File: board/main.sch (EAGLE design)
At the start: 58 parts, among them IC1 ATMEGA48/88/168-AU, IC2 LM386N-1, J1 AVR_SPI_PRG_6PTH, Q2 MOSFET-NCHANNELSMD, Q3 MOSFET-NCHANNELSMD, U1 AT24C1024B-8S2, U2 AT24C1024B-8S2

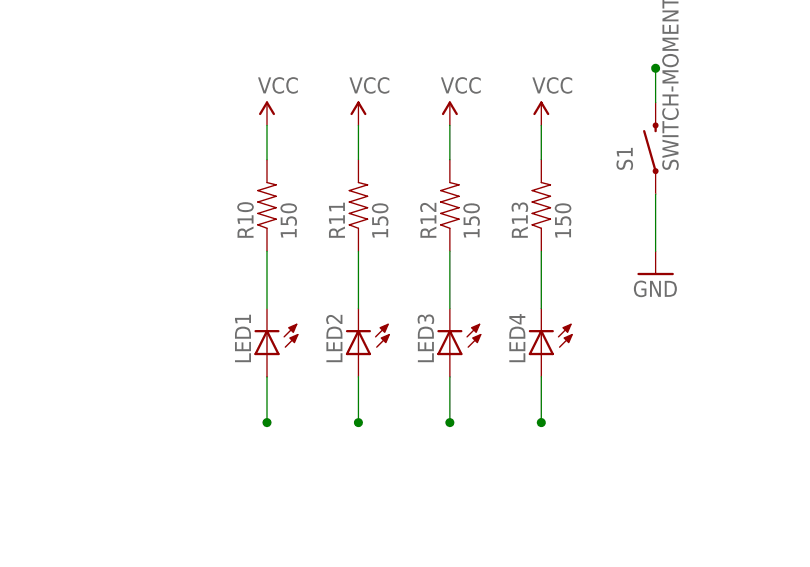
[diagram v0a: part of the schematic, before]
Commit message: Fixed the TWI interface
Seems there was a problem with the waiting for-i2c-logic.  Fixed and now it's working.  Yippie.  SO MUCH WASTED TIME.  Ugh.
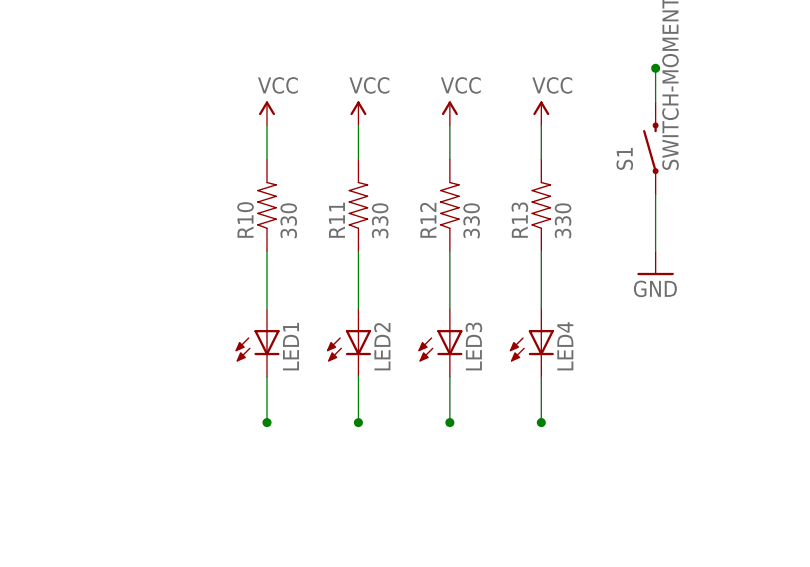
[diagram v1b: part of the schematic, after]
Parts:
- R10, R11, R12, R13: value 150 -> 330
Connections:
- net LED1: now also LED1.C; no longer LED1.A
- net LED2: now also LED2.C; no longer LED2.A
- net LED3: now also LED3.C; no longer LED3.A
- net LED4: now also LED4.C; no longer LED4.A
- net N$10: now also LED1.A, R10.1; no longer LED4.C, R13.1
- net N$11: now also LED2.A, R11.1; no longer LED3.C, R12.1
- net N$13: now also LED3.A, R12.1; no longer LED2.C, R11.1
- net N$14: now also LED4.A, R13.1; no longer LED1.C, R10.1
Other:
- moved on the sheet: LED1, LED2, LED3, LED4
